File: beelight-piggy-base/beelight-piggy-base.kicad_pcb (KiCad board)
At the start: 2 copper layers, 55 x 55 mm, 67 parts, among them J10 USB C power only, J11 ExtWSSolderPads, J3 BatSolderPads, J4 WS2812_ext, J7 DevSide, Q1 AO3400A, SW1 SW_Push, U2 BMA253, U3 TPS22917LDBV, U4 rysta, U5 VEML3328, U6 TSOP382xx, U7 MP2667, U8 BQ27421-G1

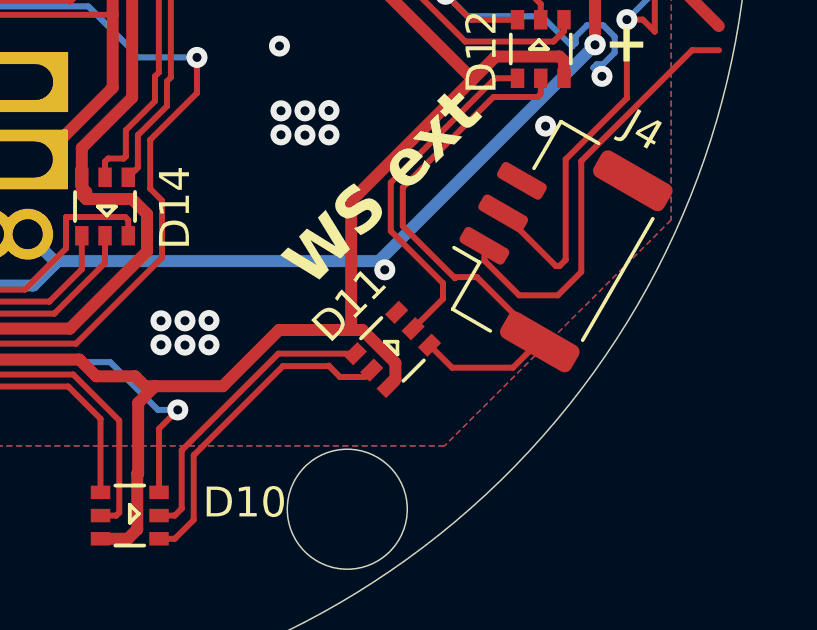
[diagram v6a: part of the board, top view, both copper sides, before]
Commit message: tius feedback 2 - fix drc issues
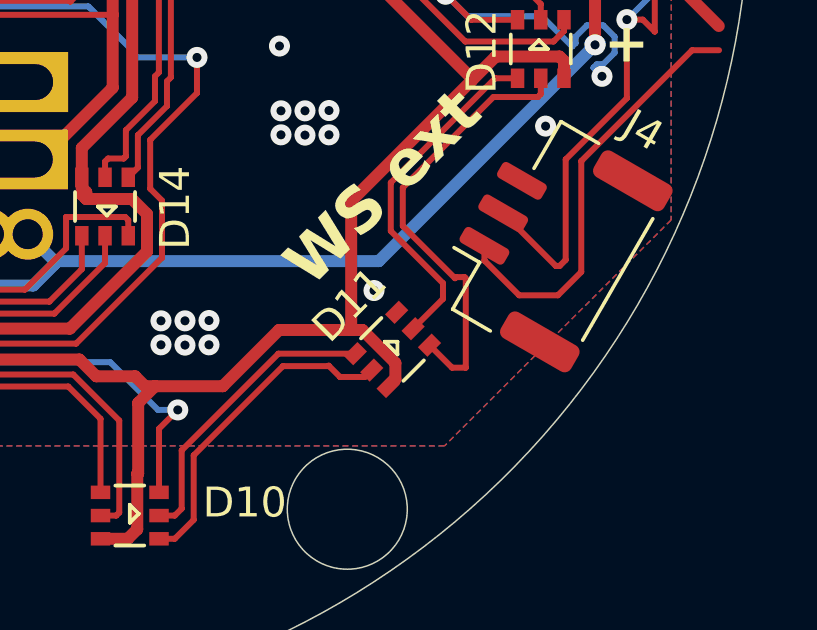
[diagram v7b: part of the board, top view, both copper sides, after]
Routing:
- net Net-(D11-DO): track 18.1 -> 15.0 mm
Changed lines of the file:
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@@
 	)
 	(via
-		(at 170.585417 108.0125)
+		(at 170.225417 108.7025)
 		(size 0.7)
 		(drill 0.3)
@@
 	)
 	(segment
-		(start 174.857679 111.274358)
-		(end 175.543209 110.588828)
-		(width 0.2)
-		(layer "F.Cu")
-		(net "Net-(D11-DO)")
-	)
-	(segment
 		(start 171.185417 106.5525)
 		(end 171.185417 105.2725)
@@
 	)
 	(segment
-		(start 175.543209 110.142986)
-		(end 173.655597 108.255374)
-		(width 0.2)
-		(layer "F.Cu")
-		(net "Net-(D11-DO)")
-	)
-	(segment
 		(start 175.785417 102.1525)
 		(end 175.785417 101.6275)
@@
 	)
 	(segment
-		(start 173.655597 108.255374)
+		(start 173.245417 108.255374)
 		(end 172.962542 108.255374)
 		(width 0.2)
@@
 	)
 	(segment
-		(start 172.828249 111.274358)
-		(end 174.857679 111.274358)
+		(start 173.285417 111.274358)
+		(end 173.285417 108.295374)
 		(width 0.2)
 		(layer "F.Cu")
@@
 	)
 	(segment
-		(start 175.543209 110.588828)
-		(end 175.543209 110.142986)
+		(start 172.828249 111.274358)
+		(end 173.285417 111.274358)
 		(width 0.2)
 		(layer "F.Cu")
@@
 		(width 0.2)
 		(layer "F.Cu")
+		(net "Net-(D11-DO)")
+	)
+	(segment
+		(start 173.285417 108.295374)
+		(end 173.245417 108.255374)
+		(width 0.2)
+		(layer "F.Cu")

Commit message: tius feedback 2 - copper cleanup
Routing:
- net BAT: track 66.9 -> 62.5 mm
- net VLED: track 61.9 -> 58.5 mm
- net Net-(D1-VDD): track 300.1 -> 297.4 mm
- net SDA: track 66.5 -> 64.8 mm
- net Net-(D22-DO): track 69.7 -> 69.1 mm
